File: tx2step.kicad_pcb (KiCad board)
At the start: 2 copper layers, 86.4 x 31.8 mm, 58 parts, among them CON1 BARREL_JACK, IC3 TPS61202, IC4 DRV8834, IC5 DRV8834, J1 Prog, J2 8P8C, J3 CHASSIS_SWITCHES, J4 6P4Cx2, SW1 SW_DIP_x02, U1 ATmega328P-MMH, U2 MCP73871-2AA, Y1 16 MHz

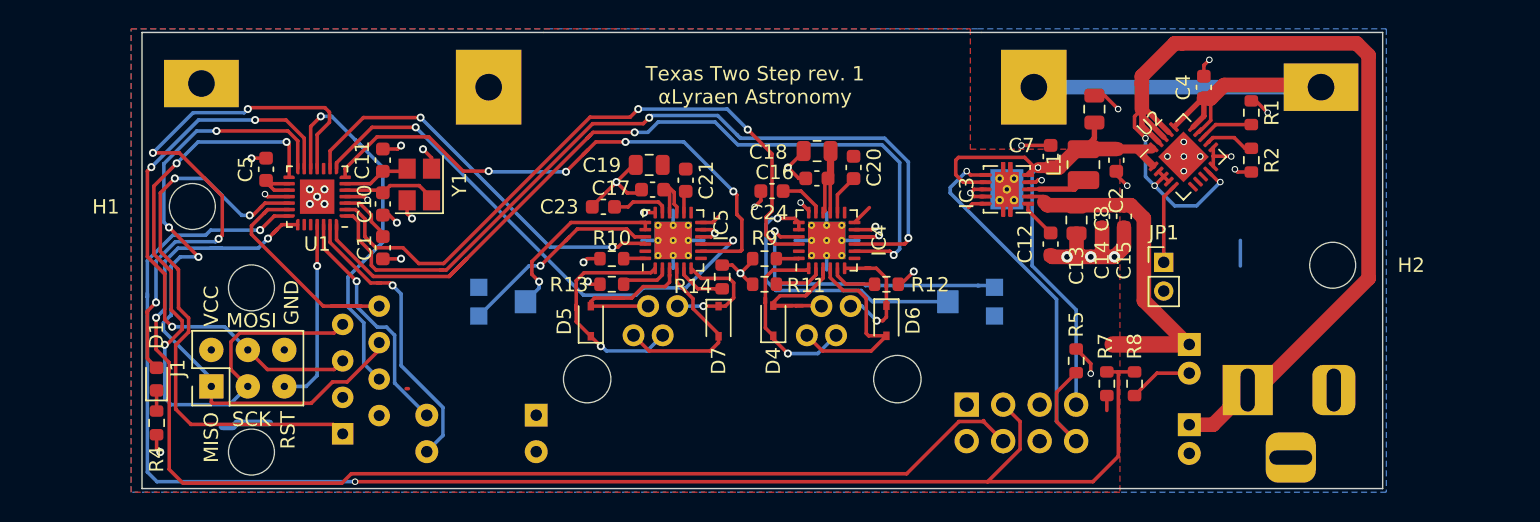
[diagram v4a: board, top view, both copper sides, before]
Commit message: Add separate uC for charge status LEDs
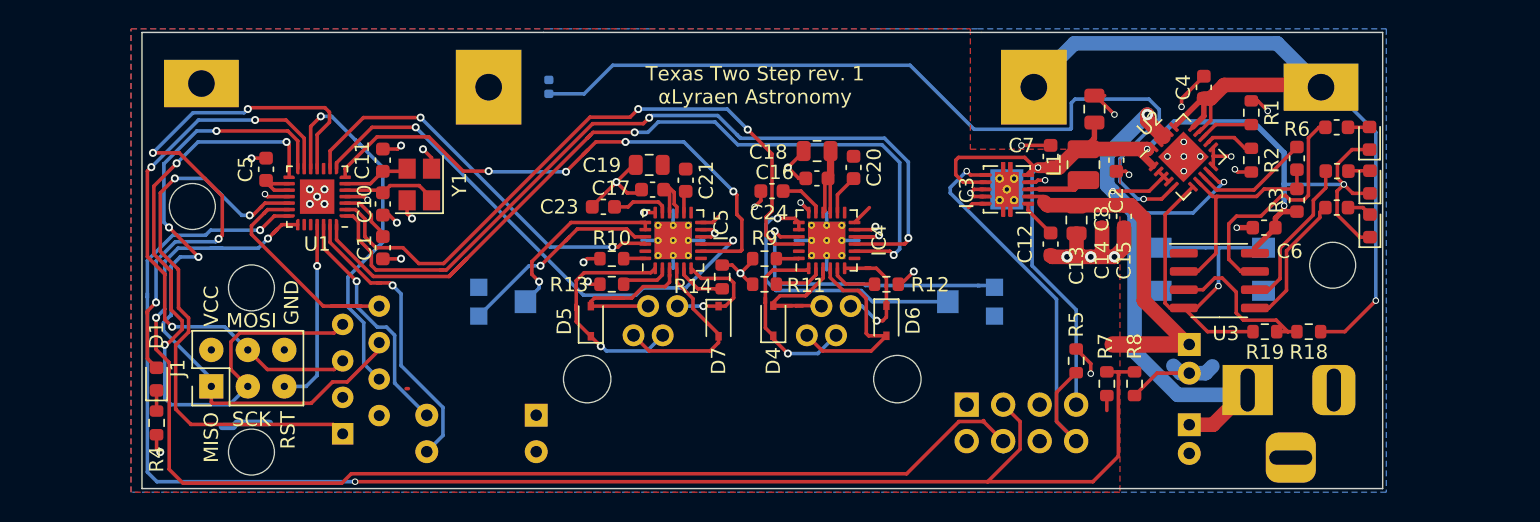
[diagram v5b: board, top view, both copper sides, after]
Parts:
- removed JP1: THERM, Connector_PinHeader_2.00mm:PinHeader_1x02_P2.00mm_Vertical
- added C6: 100nF, Capacitor_SMD:C_0603_1608Metric, F.Cu at (186.6, 71.2)
- added D2: CHARGE_1, LED_SMD:LED_0603_1608Metric, F.Cu at (193.9, 65.0)
- added D3: CHARGE_2, LED_SMD:LED_0603_1608Metric, F.Cu at (193.9, 68.1)
- added D8: CHARGE_3, LED_SMD:LED_0603_1608Metric, F.Cu at (193.9, 71.1)
- added R15: 2KΩ, Resistor_SMD:R_0603_1608Metric, F.Cu at (191.6, 64.3)
- added R16: 2KΩ, Resistor_SMD:R_0603_1608Metric, F.Cu at (191.6, 67.3)
- added R17: 2KΩ, Resistor_SMD:R_0603_1608Metric, F.Cu at (191.6, 69.8)
- added R18: 10KΩ, Resistor_SMD:R_0603_1608Metric, F.Cu at (189.7, 78.5)
- added R19: 10KΩ, Resistor_SMD:R_0603_1608Metric, F.Cu at (186.6, 78.5)
- added R3: 10KΩ, Resistor_SMD:R_0603_1608Metric, F.Cu at (188.8, 69.3)
- added R6: 1KΩ, Resistor_SMD:R_0603_1608Metric, F.Cu at (188.8, 66.4)
- added SW2: SW_Push_Dual, Button_Switch_SMD:SW_SPST_TL3305A, B.Cu at (182.9, 74.1)
- added TH1: NTC 10KΩ, Resistor_SMD:R_0402_1005Metric, B.Cu at (136.8, 61.4)
- added U3: ATtiny25V-10SSU, Package_SO:SOIC-8_3.9x4.9mm_P1.27mm, F.Cu at (183.4, 74.9)
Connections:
- net Net-(BT1-Pad1) renamed +BATT
- CON1 pad 3: (no net) -> GND
- U2 pad 6: (no net) -> /TINY_GND
- U2 pad 7: (no net) -> /CHARGE_COMPLETE
- U2 pad 8: (no net) -> /CHARGE_PROGRESS
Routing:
- net Net-(TH1-Pad1): track 5.56 -> 58.1 mm, vias 0 -> 1
- net /REG_IN: track 41.8 -> 75.8 mm, vias 1 -> 4
- net /TINY_GND: track 0.00 -> 28.8 mm, vias 0 -> 1
- net +5V: track 74.5 -> 48.9 mm
- net +BATT: track 42.3 -> 66.5 mm, vias 0 -> 1
- net Net-(R15-Pad2): track 0.00 -> 16.7 mm
- net /CHARGE_COMPLETE: track 0.00 -> 15.6 mm
- net Net-(R18-Pad2): track 0.00 -> 11.4 mm
- net Net-(R16-Pad1): track 0.00 -> 10.9 mm
- net Net-(R17-Pad2): track 0.00 -> 9.63 mm
- net /CHARGE_PROGRESS: track 0.00 -> 8.16 mm
- net GND: track 104.4 -> 109.0 mm, vias 44 -> 45
- net Net-(D8-Pad2): track 0.00 -> 1.72 mm
- net Net-(D3-Pad2): track 0.00 -> 1.51 mm
- net Net-(D2-Pad2): track 0.00 -> 1.47 mm

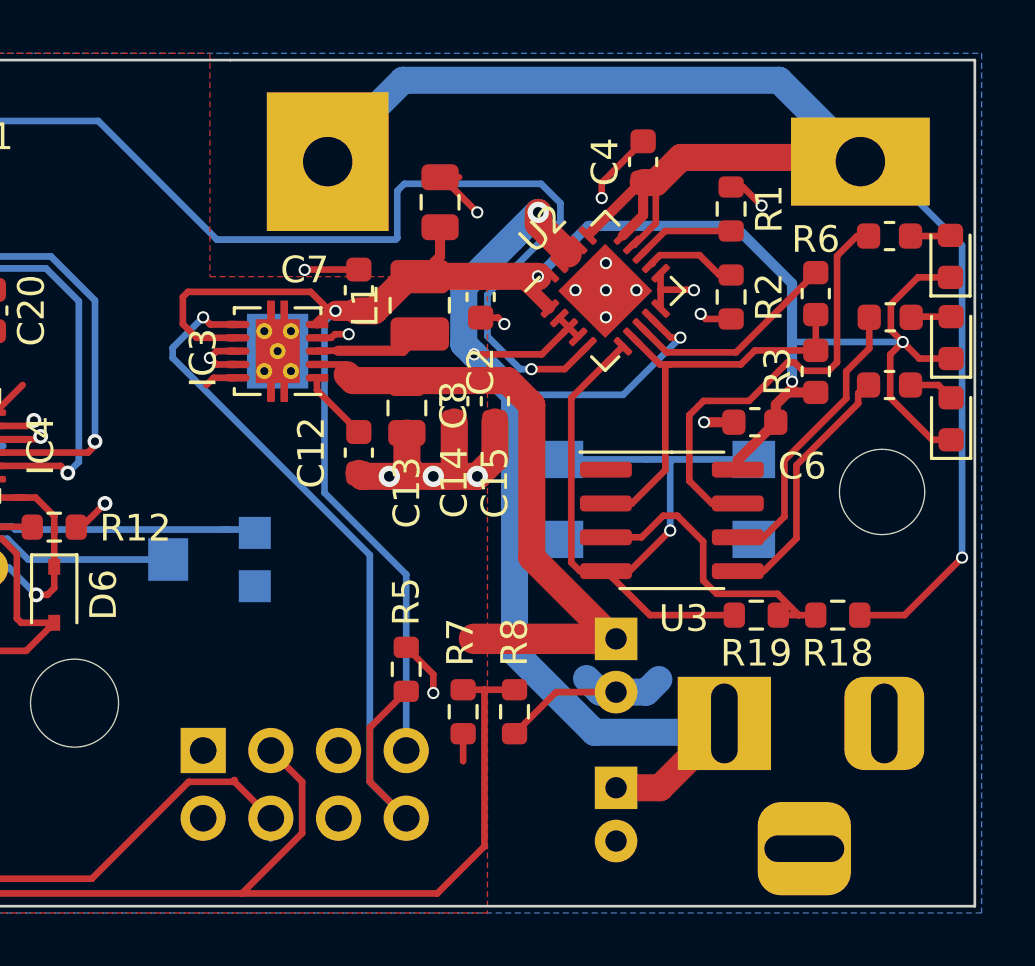
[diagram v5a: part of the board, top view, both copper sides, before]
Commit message: Add resistor divider to TPS61202 UVLO pin
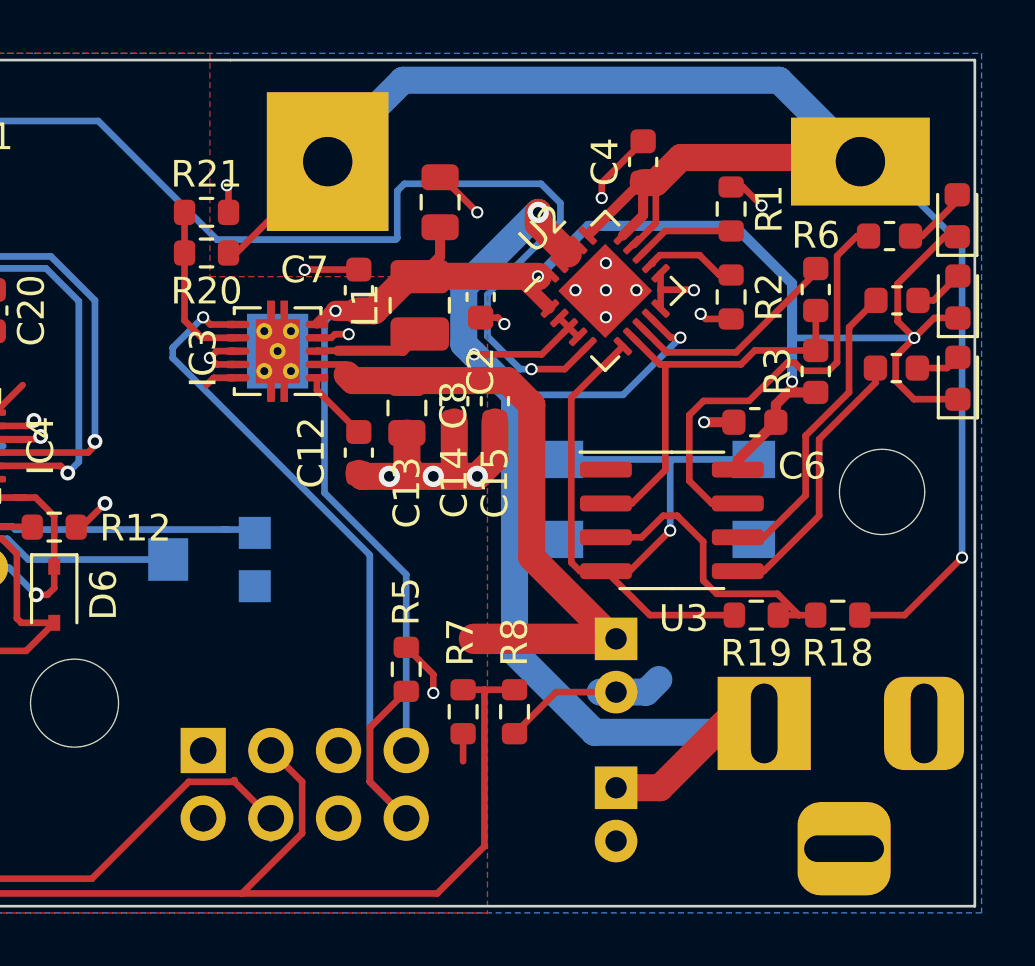
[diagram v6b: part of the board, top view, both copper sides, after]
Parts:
- added R20: 10KΩ, Resistor_SMD:R_0603_1608Metric, F.Cu at (166.0, 64.9)
- added R21: 910Ω, Resistor_SMD:R_0603_1608Metric, F.Cu at (166.0, 63.4)
- moved D2 1.55 mm to (194.2, 63.5)
- moved D3 1.55 mm to (194.2, 66.5)
- moved D8 1.55 mm to (194.2, 69.6)
- moved CON1 1.49 mm to (186.9, 82.5)
- moved R16 0.68 mm to (191.9, 66.7)
- moved R17 0.68 mm to (191.9, 69.2)
- moved R6 0.15 mm to (188.8, 66.3)
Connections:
- IC3 pad 7: /REG_IN -> Net-(IC3-Pad7)
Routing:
- net /REG_IN: track 75.8 -> 67.2 mm
- net Net-(IC3-Pad7): track 0.00 -> 6.34 mm
- net +BATT: track 66.5 -> 71.7 mm
- net Net-(D2-Pad2): track 1.47 -> 2.53 mm
- net Net-(R16-Pad1): track 10.9 -> 11.6 mm
- net Net-(R17-Pad2): track 9.63 -> 10.3 mm
- net GND: track 109.0 -> 108.6 mm, vias 45 -> 46

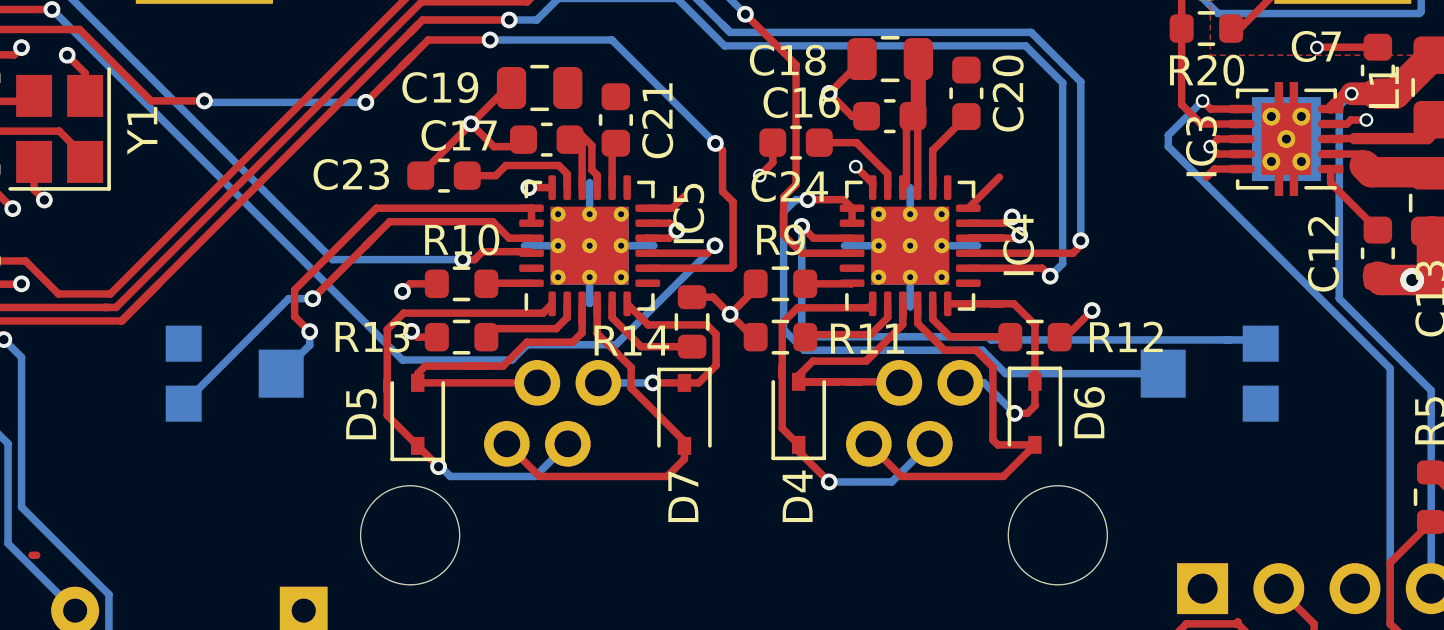
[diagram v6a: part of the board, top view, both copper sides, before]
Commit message: Reverse trimpot pins
Make clockwise increase the ILIM voltage
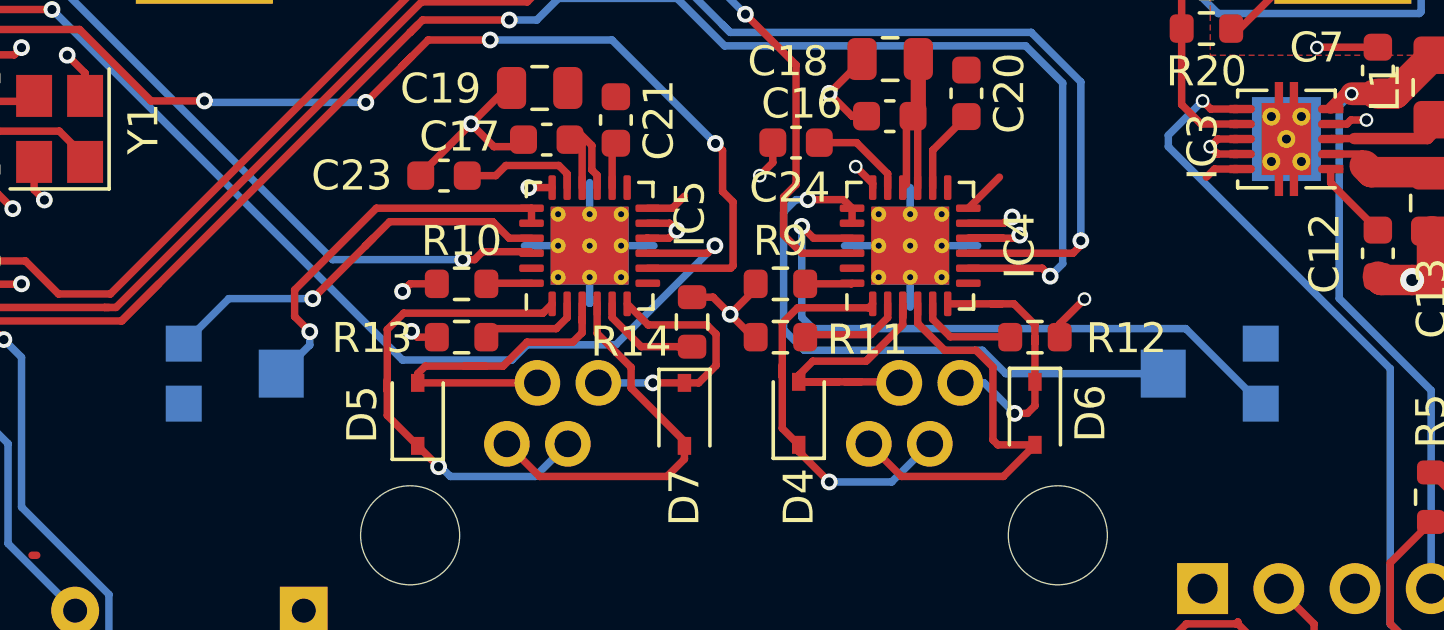
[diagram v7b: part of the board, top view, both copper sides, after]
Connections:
- RV1 pad 1: Net-(IC4-Pad21) -> GND
- RV1 pad 3: GND -> Net-(IC4-Pad21)
- RV2 pad 1: Net-(IC5-Pad21) -> GND
- RV2 pad 3: GND -> Net-(IC5-Pad21)
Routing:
- net Net-(IC5-Pad21): track 14.7 -> 13.9 mm
- net GND: track 108.6 -> 109.2 mm
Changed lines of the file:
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@@
     (thickness 1.6)
     (drawings 36)
-    (tracks 945)
+    (tracks 942)
     (zones 0)
     (modules 73)
@@
     (add_net "Net-(IC3-Pad3)")
     (add_net "Net-(IC3-Pad7)")
+    (add_net "Net-(IC4-Pad13)")
     (add_net "Net-(IC4-Pad19)")
     (add_net "Net-(IC4-Pad2)")
     (add_net "Net-(IC4-Pad21)")
+    (add_net "Net-(IC4-Pad23)")
     (add_net "Net-(IC4-Pad24)")
     (add_net "Net-(IC4-Pad5)")
+    (add_net "Net-(IC4-Pad7)")
+    (add_net "Net-(IC5-Pad13)")
     (add_net "Net-(IC5-Pad19)")
     (add_net "Net-(IC5-Pad2)")
     (add_net "Net-(IC5-Pad21)")
+    (add_net "Net-(IC5-Pad23)")
     (add_net "Net-(IC5-Pad24)")
     (add_net "Net-(IC5-Pad5)")
+    (add_net "Net-(IC5-Pad7)")
     (add_net "Net-(R1-Pad2)")
     (add_net "Net-(R15-Pad2)")
@@
     (add_net "Net-(R2-Pad1)")
     (add_net "Net-(TH1-Pad1)")
+    (add_net "Net-(U1-Pad10)")
+    (add_net "Net-(U1-Pad23)")
+    (add_net "Net-(U1-Pad24)")
+    (add_net "Net-(U3-Pad1)")
     (add_net VCC)
   )
@@
       (net 19 "Net-(IC5-Pad19)"))
     (pad 3 smd rect (at -1.8 -1) (size 1.2 1.2) (layers B.Cu B.Paste B.Mask)
-      (net 1 GND))
-    (pad 1 smd rect (at -1.8 1) (size 1.2 1.2) (layers B.Cu B.Paste B.Mask)
       (net 38 "Net-(IC5-Pad21)"))
+    (pad 1 smd rect (at -1.8 1) (size 1.2 1.2) (layers B.Cu B.Paste B.Mask)
+      (net 1 GND))
     (model ${KISYS3DMOD}/Potentiometer_SMD.3dshapes/Potentiometer_Bourns_TC33X_Vertical.wrl
       (at (xyz 0 0 0))
@@
       (net 45 "Net-(IC4-Pad19)"))
     (pad 3 smd rect (at -1.8 -1 180) (size 1.2 1.2) (layers B.Cu B.Paste B.Mask)
-      (net 1 GND))
-    (pad 1 smd rect (at -1.8 1 180) (size 1.2 1.2) (layers B.Cu B.Paste B.Mask)
       (net 44 "Net-(IC4-Pad21)"))
+    (pad 1 smd rect (at -1.8 1 180) (size 1.2 1.2) (layers B.Cu B.Paste B.Mask)
+      (net 1 GND))
     (model ${KISYS3DMOD}/Potentiometer_SMD.3dshapes/Potentiometer_Bourns_TC33X_Vertical.wrl
       (at (xyz 0 0 0))
@@
   (segment (start 181.356 81.375) (end 179.106099 81.375) (width 0.25) (layer F.Cu) (net 1) (status 10))
   (segment (start 161.099 75.184) (end 161.29 75.184) (width 0.25) (layer F.Cu) (net 1) (status 30))
-  (via (at 162.179 74.295) (size 0.5588) (drill 0.3048) (layers F.Cu B.Cu) (net 1))
-  (segment (start 161.29 75.184) (end 162.179 74.295) (width 0.25) (layer F.Cu) (net 1) (status 10))
   (via (at 154.3 69.5) (size 0.4572) (drill 0.3048) (layers F.Cu B.Cu) (net 1))
   (segment (start 154.8655 70.0655) (end 154.3 69.5) (width 0.25) (layer F.Cu) (net 1) (status 10))
@@
   (segment (start 138.76399 71.33601) (end 137.95 72.15) (width 0.25) (layer F.Cu) (net 38))
   (segment (start 143.4925 71.886) (end 142.74999 71.886) (width 0.25) (layer F.Cu) (net 38) (status 10))
-  (segment (start 135.4 73.9) (end 136.2 73.9) (width 0.25) (layer B.Cu) (net 38))
-  (segment (start 131.9 77.4) (end 135.4 73.9) (width 0.25) (layer B.Cu) (net 38) (status 10))
+  (segment (start 133.4 73.9) (end 131.9 75.4) (width 0.25) (layer B.Cu) (net 38))
+  (segment (start 136.2 73.9) (end 133.4 73.9) (width 0.25) (layer B.Cu) (net 38))
   (segment (start 170.131 70.042) (end 171.704 71.615) (width 0.25) (layer F.Cu) (net 39) (status 20))
   (segment (start 170.131 69.58) (end 170.131 70.042) (width 0.25) (layer F.Cu) (net 39) (status 10))
@@
   (via (at 152.5 71.4904) (size 0.5588) (drill 0.3048) (layers F.Cu B.Cu) (net 44))
   (segment (start 154.178 71.886) (end 152.8956 71.886) (width 0.25) (layer F.Cu) (net 44) (status 10))
-  (segment (start 158.811409 75.274999) (end 158.707399 75.170989) (width 0.25) (layer B.Cu) (net 44))
-  (segment (start 152.5 74.9) (end 152.5 71.4904) (width 0.25) (layer B.Cu) (net 44))
-  (segment (start 152.770989 75.170989) (end 152.5 74.9) (width 0.25) (layer B.Cu) (net 44))
-  (segment (start 158.707399 75.170989) (end 152.770989 75.170989) (width 0.25) (layer B.Cu) (net 44))
-  (segment (start 167.674999 75.274999) (end 167.8 75.4) (width 0.25) (layer B.Cu) (net 44) (status 30))
-  (segment (start 166.625001 75.274999) (end 167.674999 75.274999) (width 0.25) (layer B.Cu) (net 44) (status 20))
-  (segment (start 166.774999 75.274999) (end 166.625001 75.274999) (width 0.25) (layer B.Cu) (net 44))
-  (segment (start 166.625001 75.274999) (end 158.811409 75.274999) (width 0.25) (layer B.Cu) (net 44))
+  (segment (start 167.674999 75.274999) (end 167.8 75.4) (width 0.25) (layer B.Cu) (net 1) (status 30))
+  (via (at 161.925 73.914) (size 0.4572) (drill 0.3048) (layers F.Cu B.Cu) (net 1))
+  (segment (start 161.099 74.74) (end 161.925 73.914) (width 0.25) (layer F.Cu) (net 1))
+  (segment (start 161.099 75.184) (end 161.099 74.74) (width 0.25) (layer F.Cu) (net 1))
+  (segment (start 165.299401 74.899401) (end 152.877401 74.899401) (width 0.25) (layer B.Cu) (net 44))
+  (segment (start 167.8 77.4) (end 165.299401 74.899401) (width 0.25) (layer B.Cu) (net 44))
+  (segment (start 152.5 74.522) (end 152.5 71.4904) (width 0.25) (layer B.Cu) (net 44))
+  (segment (start 152.877401 74.899401) (end 152.5 74.522) (width 0.25) (layer B.Cu) (net 44))
   (segment (start 154.178 70.886) (end 154.178 71.386) (width 0.25) (layer F.Cu) (net 45) (status 30))
   (via (at 152.7 70.6) (size 0.5588) (drill 0.3048) (layers F.Cu B.Cu) (net 45))
@@
   (segment (start 158.520999 75.620999) (end 152.584588 75.620998) (width 0.25) (layer B.Cu) (net 45))
   (segment (start 159.220989 75.170989) (end 159.45 75.4) (width 0.25) (layer F.Cu) (net 46) (status 30))
-  (segment (start 157.449439 75.170989) (end 159.220989 75.170989) (width 0.25) (layer F.Cu) (net 46) (status 20))
   (segment (start 156.8655 74.0735) (end 156.8655 74.58705) (width 0.25) (layer F.Cu) (net 46) (status 10))
   (segment (start 156.8655 74.58705) (end 157.449439 75.170989) (width 0.25) (layer F.Cu) (net 46))
-  (segment (start 152.6975 75.1) (end 152.6135 75.184) (width 0.25) (layer F.Cu) (net 47) (status 30))
+  (segment (start 157.449439 75.170989) (end 159.220989 75.170989) (width 0.25) (layer F.Cu) (net 46) (status 20))
   (segment (start 154.799522 75.1) (end 152.6975 75.1) (width 0.25) (layer F.Cu) (net 47) (status 20))
   (segment (start 155.3655 74.0735) (end 155.3655 74.534022) (width 0.25) (layer F.Cu) (net 47) (status 10))
